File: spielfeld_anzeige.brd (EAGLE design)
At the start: 100 x 80 mm, 22 parts, among them IC1 UDN2981A, IC2 UDN2981A, IC3 74HC595N, IC4 74HC595N, IC5 74HC595N

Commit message: Schematic mit 3 Digits fertig
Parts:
- removed R2: (no value), rcl:R3216
- JP1: value (none) -> 8 Pin
- L1, L2: value (none) -> red
- R1: value (none) -> 56
- R3: value (none) -> 10k
- moved JP1 181.4 mm to (21.6, 1.27), turned to 180 degrees
- moved L1 174.4 mm to (31.8, 66.0), turned to 90 degrees
- moved L2 168.4 mm to (31.8, 47.0), turned to 90 degrees
- moved D2 124.4 mm to (53.3, 57.1)
- moved D1 123.3 mm to (91.4, 57.1)
- moved D3 119.9 mm to (8.89, 57.1)
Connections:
- removed net GND1: C1.2
- removed net GND2: C3.2
- removed net N$18: L2.A, R2.1
- removed net N$19: L1.A, R1.1
- net +5V: now also IC1.9, IC2.9; no longer IC1.10, IC2.10
- net COLON_OUT: now also IC2.11, R1.2; no longer RN4.8
- net GND: now also C1.2, C3.2, IC1.10, IC2.10; no longer IC1.9, IC2.9, L2.K
- net N$1: now also L1.A, L2.K; no longer ICL1.16
- net N$13: now also L2.A, R1.1; no longer IC2.11, RN4.7
- net R1_OUT: now also D2.9, D3.9, ICL1.16
- net R2_OUT: now also D2.14, D3.14, ICL1.15
- net R3_OUT: now also D2.8, D3.8, ICL1.14
- net R4_OUT: now also D2.12, D2.5, D3.12, D3.5, ICL1.13
- net R5_OUT: now also D2.1, D3.1, ICL1.12
- net R6_OUT: now also D2.7, D3.7, ICL1.11
- net R7_OUT: now also D2.2, D3.2, ICL1.10

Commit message: Reduced to 2 digits on board. Bom updated.
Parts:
- removed D3: TA20-11HWA, display-kingbright:TA20-11HWA
- removed RN4: 180, resistor-sil:SIL8
- moved C1 267.6 mm to (63.5, 54.6), turned to 90 degrees
- moved C3 252.2 mm to (15.2, 54.6), turned to 90 degrees
- moved IC3 228.5 mm to (72.4, 54.6), turned to 180 degrees
- moved IC4 219.1 mm to (48.3, 54.6), turned to 180 degrees
- moved R3 217.2 mm to (5.08, 12.7), turned to 270 degrees
- moved IC5 212.9 mm to (24.1, 54.6), turned to 180 degrees
- moved R1 200.4 mm to (50.8, 35.6), turned to 270 degrees
- moved RN2 176.0 mm to (51.3, 29.4), turned to 180 degrees
- moved RN1 175.5 mm to (51.3, 33.3), turned to 180 degrees
- moved C2 172.3 mm to (39.4, 54.6), turned to 90 degrees
- moved RN3 166.1 mm to (26.3, 33.5), turned to 180 degrees
- moved IC2 163.1 mm to (25.4, 41.9), turned to 180 degrees
- moved ICL1 87.1 mm to (74.9, 41.9), turned to 180 degrees
- moved D1 68.7 mm to (22.9, 53.3)
- moved IC1 59.9 mm to (49.5, 41.9), turned to 180 degrees
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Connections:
- removed net D3_C1_OUT: D3.13, RN3.6
- removed net D3_C2_OUT: D3.3, RN3.8
- removed net D3_C3_OUT: D3.11, D3.4, RN4.2
- removed net D3_C4_OUT: D3.10, RN4.4
- removed net D3_C5_OUT: D3.6, RN4.6
- removed net N$10: IC2.14, RN4.1
- removed net N$11: IC2.13, RN4.3
- removed net N$12: IC2.12, RN4.5
- removed net N$8: IC2.16, RN3.5
- removed net N$9: IC2.15, RN3.7
- net COLON_OUT: now also IC2.16; no longer IC2.11
- net R1_OUT: no longer D3.9
- net R2_OUT: no longer D3.14
- net R3_OUT: no longer D3.8
- net R4_OUT: no longer D3.12, D3.5
- net R5_OUT: no longer D3.1
- net R6_OUT: no longer D3.7
- net R7_OUT: no longer D3.2
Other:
- board size 100 x 80 mm -> 100 x 85 mm

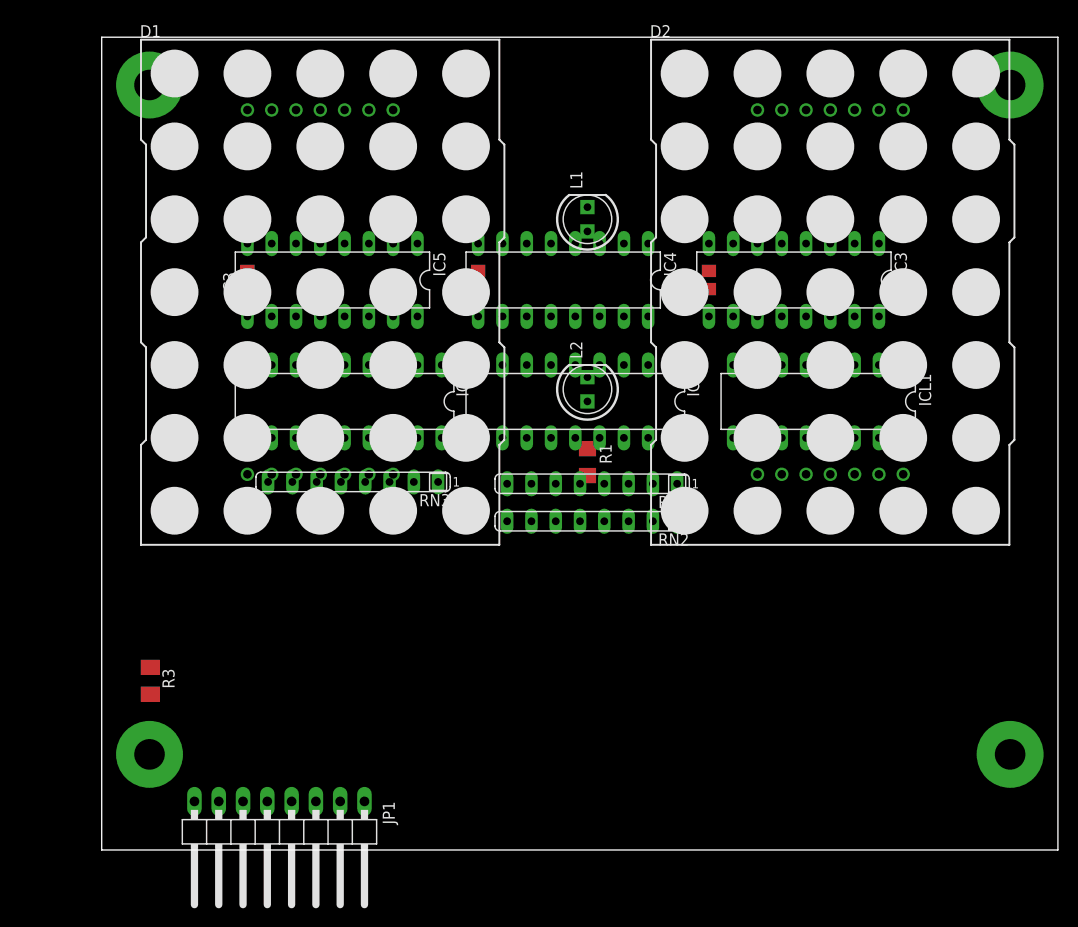
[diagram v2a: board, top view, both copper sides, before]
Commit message: PCB design finished with tht parts on backside of board
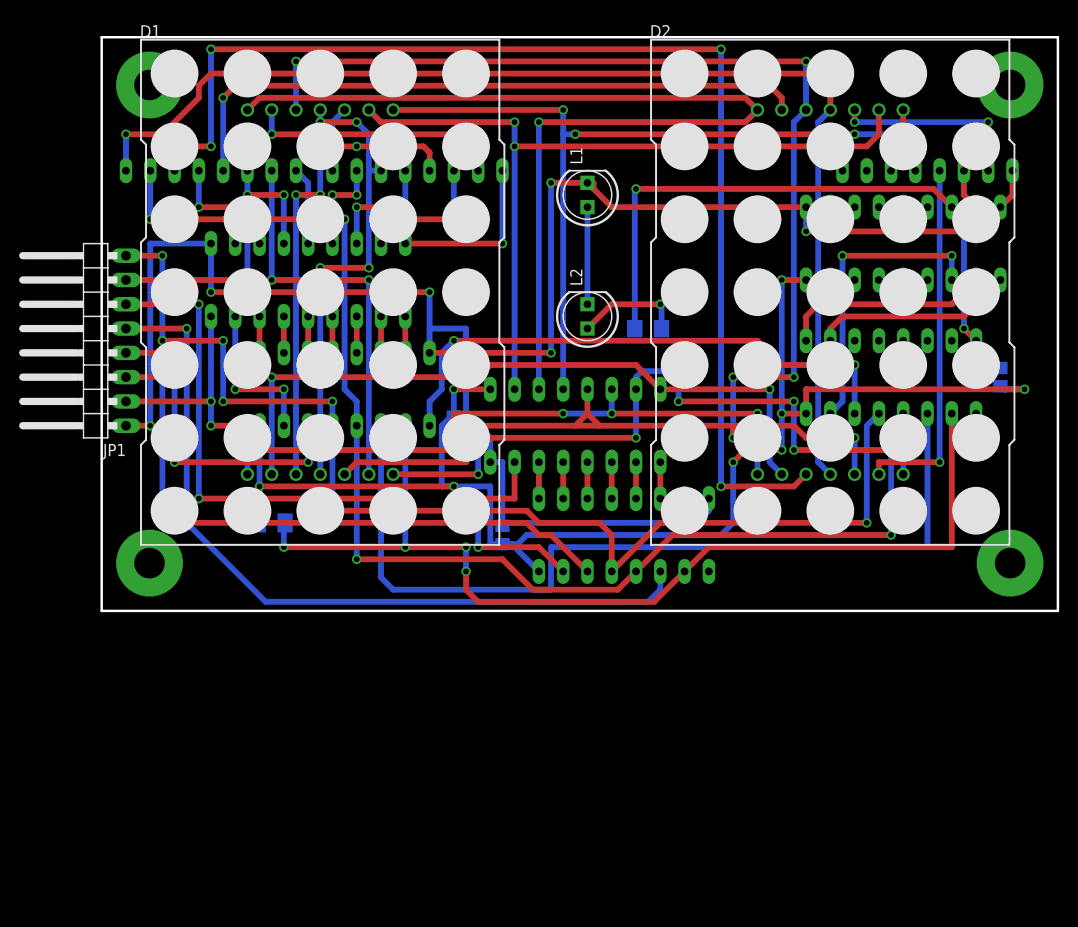
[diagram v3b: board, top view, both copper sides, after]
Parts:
- moved C3 79.4 mm to (94.0, 44.5), flipped to the bottom
- moved RN3 68.3 mm to (86.4, 66.0), flipped to the bottom, turned to 0 degrees
- moved IC2 60.7 mm to (83.8, 58.4), flipped to the bottom, turned to 0 degrees
- moved IC5 59.3 mm to (82.5, 44.5), flipped to the bottom
- moved JP1 55.7 mm to (-1.27, 48.3), turned to 90 degrees
- moved RN2 54.2 mm to (11.4, 66.0), flipped to the bottom, turned to 0 degrees
- moved RN1 37.5 mm to (33.0, 66.0), flipped to the bottom, turned to 0 degrees
- moved C1 34.3 mm to (41.9, 27.9), flipped to the bottom
- moved IC3 32.1 mm to (54.6, 27.9), flipped to the bottom
- moved IC1 30.7 mm to (21.6, 54.6), flipped to the bottom, turned to 0 degrees
- moved IC4 25.6 mm to (25.4, 43.2), flipped to the bottom
- moved ICL1 25.5 mm to (49.5, 39.4), flipped to the bottom, turned to 0 degrees
- moved R3 20.8 mm to (17.8, 29.2), flipped to the bottom, turned to 0 degrees
- moved C2 15.5 mm to (36.8, 39.4), flipped to the bottom, turned to 270 degrees
- moved R1 15.3 mm to (57.1, 49.5), flipped to the bottom, turned to 0 degrees
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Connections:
- net D2_C5_DATA renamed D2_C5
- net R4_DATA renamed N$11
- removed net COLON_DATA: IC2.8, IC5.7
- removed net D1_C1_DATA: IC1.1, IC4.15
- removed net D1_C2_DATA: IC1.2, IC4.1
- removed net D1_C3_DATA: IC1.3, IC4.2
- removed net D1_C4_DATA: IC1.4, IC4.3
- removed net D1_C5_DATA: IC1.5, IC4.4
- removed net D2_C1_DATA: IC1.6, IC4.5
- removed net D2_C2_DATA: IC1.7, IC4.6
- removed net D2_C3_DATA: IC1.8, IC4.7
- removed net D2_C4_DATA: IC2.1, IC5.15
- removed net D3_C1_DATA: IC2.3, IC5.2
- removed net D3_C2_DATA: IC2.4, IC5.3
- removed net D3_C3_DATA: IC2.5, IC5.4
- removed net D3_C4_DATA: IC2.6, IC5.5
- removed net D3_C5_DATA: IC2.7, IC5.6
- removed net R1_DATA: IC3.15, ICL1.1
- removed net R2_DATA: IC3.1, ICL1.2
- removed net R3_DATA: IC3.2, ICL1.3
- removed net R5_DATA: IC3.4, ICL1.5
- removed net R6_DATA: IC3.5, ICL1.6
- removed net R7_DATA: IC3.6, ICL1.7
- new net COLON: IC2.3, IC5.15
- new net D1_C1: IC1.1, IC4.7
- new net D1_C2: IC1.2, IC4.6
- new net D1_C3: IC1.3, IC4.5
- new net D1_C4: IC1.4, IC4.4
- new net D1_C5: IC1.5, IC4.3
- new net D2_C1: IC1.6, IC4.2
- new net D2_C2: IC1.7, IC4.1
- new net D2_C3: IC1.8, IC4.15
- new net D2_C4: IC2.1, IC5.2
- new net N$10: IC3.2, ICL1.5
- new net N$12: IC3.4, ICL1.3
- new net N$18: IC3.5, ICL1.2
- new net N$21: IC3.6, ICL1.1
- new net N$8: IC3.15, ICL1.7
- new net N$9: IC3.1, ICL1.6
- net R1_OUT: now also ICL1.10; no longer ICL1.16
- net R2_OUT: now also ICL1.11; no longer ICL1.15
- net R3_OUT: now also ICL1.12; no longer ICL1.14
- net R5_OUT: now also ICL1.14; no longer ICL1.12
- net R6_OUT: now also ICL1.15; no longer ICL1.11
- net R7_OUT: now also ICL1.16; no longer ICL1.10
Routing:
- net GND: track 0.00 -> 210.0 mm, vias 0 -> 8
- net +5V: track 0.00 -> 175.8 mm, vias 0 -> 10
- net R4_OUT: track 0.00 -> 174.1 mm, vias 0 -> 6
- net COL_SCK: track 0.00 -> 139.0 mm, vias 0 -> 3
- net RCK: track 0.00 -> 138.1 mm, vias 0 -> 5
- net D2_C2_OUT: track 0.00 -> 125.0 mm, vias 0 -> 4
- net D2_C3_OUT: track 0.00 -> 123.1 mm, vias 0 -> 1
- net !ENABLE!: track 0.00 -> 123.1 mm, vias 0 -> 7
- net !SCLR!: track 0.00 -> 106.5 mm, vias 0 -> 4
- net R2_OUT: track 0.00 -> 105.7 mm, vias 0 -> 1
- net R3_OUT: track 0.00 -> 85.1 mm, vias 0 -> 4
- net R1_OUT: track 0.00 -> 84.9 mm, vias 0 -> 2
- net ROW_SCK: track 0.00 -> 82.1 mm, vias 0 -> 1
- net R6_OUT: track 0.00 -> 73.4 mm, vias 0 -> 7
- net R7_OUT: track 0.00 -> 73.2 mm, vias 0 -> 2
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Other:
- board size 100 x 85 mm -> 100 x 60 mm
